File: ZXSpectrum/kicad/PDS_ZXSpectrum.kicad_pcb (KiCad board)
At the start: 2 copper layers, 73.7 x 70 mm, 15 parts, among them J2 PDS_IFACE, SW1 RESET, SW2 ENABLE, U1 Z8420 PIO, U2 74LS245, U3 74LS04

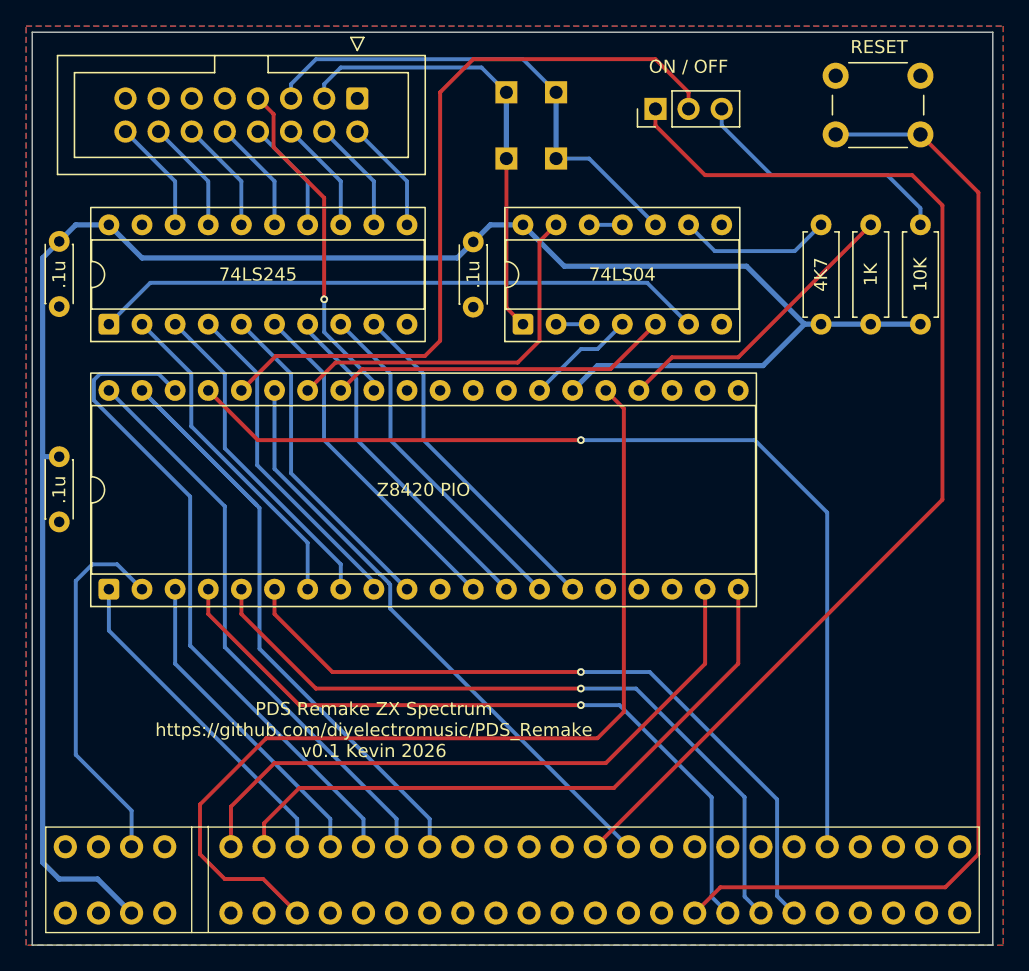
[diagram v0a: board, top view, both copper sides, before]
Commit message: Amstrad CPC
Added Amstrad CPC and updates Spectrum
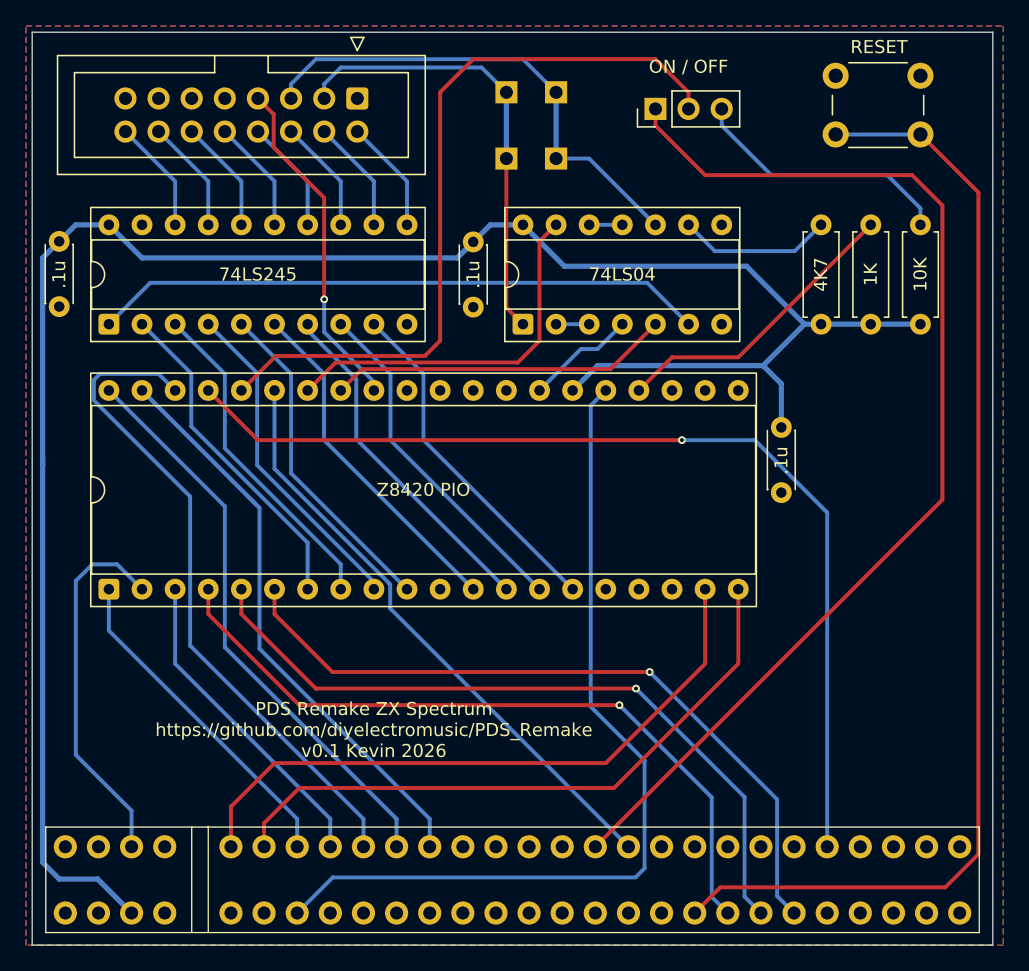
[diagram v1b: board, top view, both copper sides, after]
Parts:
- moved C1 55.4 mm to (107.4, 80.3)
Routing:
- net /CLOCK: track 73.8 -> 66.9 mm
- net VCC: track 150.2 -> 154.2 mm
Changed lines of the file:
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@@
 	(footprint "Capacitor_THT:C_Disc_D4.3mm_W1.9mm_P5.00mm"
 		(layer "F.Cu")
-		(at 52.07 82.55 -90)
+		(at 107.442 80.304 -90)
 		(descr "C, Disc series, Radial, pin pitch=5.00mm, diameter*width=4.3*1.9mm^2, Capacitor, http://www.vishay.com/docs/45233/krseries.pdf")
 		(tags "C Disc series Radial pin pitch 5.00mm diameter 4.3mm width 1.9mm Capacitor")
@@
 	)
 	(segment
+		(start 107.442 76.962)
+		(end 107.442 80.304)
+		(width 0.4)
+		(layer "B.Cu")
+		(net 1)
+	)
+	(segment
 		(start 58.42 67.31)
 		(end 55.88 64.77)
@@
 	)
 	(segment
+		(start 106.045 75.565)
+		(end 107.442 76.962)
+		(width 0.4)
+		(layer "B.Cu")
+		(net 1)
+	)
+	(segment
 		(start 82.59 67.31)
 		(end 58.42 67.31)
@@
 	)
 	(segment
-		(start 50.8 82.55)
-		(end 52.07 82.55)
-		(width 0.4)
-		(layer "B.Cu")
-		(net 1)
-	)
-	(segment
 		(start 85.13 64.77)
 		(end 83.82 66.08)
@@
 	)
 	(segment
+		(start 99.822 81.28)
+		(end 67.31 81.28)
+		(width 0.3)
+		(layer "F.Cu")
+		(net 4)
+	)
+	(segment
 		(start 67.31 81.28)
 		(end 63.5 77.47)
@@
 		(net 4)
 	)
-	(segment
-		(start 92.075 81.28)
-		(end 67.31 81.28)
-		(width 0.3)
-		(layer "F.Cu")
-		(net 4)
-	)
 	(via
-		(at 92.075 81.28)
+		(at 99.822 81.28)
 		(size 0.6)
 		(drill 0.3)
@@
 	)
 	(segment
+		(start 105.41 81.28)
+		(end 110.96 86.83)
+		(width 0.3)
+		(layer "B.Cu")
+		(net 4)
+	)
+	(segment
+		(start 99.822 81.28)
+		(end 105.41 81.28)
+		(width 0.3)
+		(layer "B.Cu")
+		(net 4)
+	)
+	(segment
 		(start 110.96 86.83)
-		(end 105.41 81.28)
-		(width 0.3)
-		(layer "B.Cu")
-		(net 4)
-	)
-	(segment
-		(start 110.96 112.46)
-		(end 110.96 86.83)
-		(width 0.3)
-		(layer "B.Cu")
-		(net 4)
-	)
-	(segment
-		(start 105.41 81.28)
-		(end 92.075 81.28)
+		(end 110.96 112.46)
 		(width 0.3)
 		(layer "B.Cu")
@@
 	)
 	(segment
+		(start 97.35 99.06)
+		(end 73.025 99.06)
+		(width 0.3)
+		(layer "F.Cu")
+		(net 12)
+	)
+	(segment
 		(start 73.025 99.06)
 		(end 68.58 94.615)
@@
 		(net 12)
 	)
-	(segment
-		(start 92.075 99.06)
-		(end 73.025 99.06)
-		(width 0.3)
-		(layer "F.Cu")
-		(net 12)
-	)
 	(via
-		(at 92.075 99.06)
+		(at 97.35 99.06)
 		(size 0.6)
 		(drill 0.3)
@@
 	)
 	(segment
-		(start 92.075 99.06)
-		(end 97.35 99.06)
+		(start 107.12 116.24)
+		(end 108.42 117.54)
+		(width 0.3)
+		(layer "B.Cu")
+		(net 12)
+	)
+	(segment
+		(start 97.35 99.06)
+		(end 107.12 108.83)
 		(width 0.3)
 		(layer "B.Cu")
@@
 	)
 	(segment
-		(start 107.12 116.24)
-		(end 108.42 117.54)
-		(width 0.3)
-		(layer "B.Cu")
-		(net 12)
-	)
-	(segment
-		(start 97.35 99.06)
-		(end 107.12 108.83)
-		(width 0.3)
-		(layer "B.Cu")
-		(net 12)
+		(start 96.3 100.33)
+		(end 71.755 100.33)
+		(width 0.3)
+		(layer "F.Cu")
+		(net 13)
+	)
+	(segment
+		(start 66.04 94.615)
+		(end 66.04 92.71)
+		(width 0.3)
+		(layer "F.Cu")
+		(net 13)
 	)
 	(segment
@@
 		(net 13)
 	)
-	(segment
-		(start 66.04 94.615)
-		(end 66.04 92.71)
-		(width 0.3)
-		(layer "F.Cu")
-		(net 13)
-	)
-	(segment
-		(start 92.075 100.33)
-		(end 71.755 100.33)
-		(width 0.3)
-		(layer "F.Cu")
-		(net 13)
-	)
 	(via
-		(at 92.075 100.33)
+		(at 96.3 100.33)
 		(size 0.6)
 		(drill 0.3)
@@
 	)
 	(segment
-		(start 92.075 100.33)
-		(end 96.3 100.33)
-		(width 0.3)
-		(layer "B.Cu")
-		(net 13)
-	)
-	(segment
 		(start 96.3 100.33)
 		(end 104.625 108.655)
@@
 	)
 	(segment
-		(start 67.715 114.935)
-		(end 64.77 114.935)
-		(width 0.3)
-		(layer "F.Cu")
+		(start 96.266 114.808)
+		(end 96.96 114.114)
+		(width 0.3)
+		(layer "B.Cu")
 		(net 14)
 	)
 	(segment
-		(start 93.345 104.14)
-		(end 95.369 102.116)
-		(width 0.3)
-		(layer "F.Cu")
+		(start 96.96 114.114)
+		(end 96.96 105.85)
+		(width 0.3)
+		(layer "B.Cu")
 		(net 14)
 	)
 	(segment
-		(start 62.865 109.22)
-		(end 67.945 104.14)
-		(width 0.3)
-		(layer "F.Cu")
+		(start 92.829 101.719)
+		(end 92.829 78.621)
+		(width 0.3)
+		(layer "B.Cu")
 		(net 14)
 	)
 	(segment
-		(start 64.77 114.935)
-		(end 62.865 113.03)
-		(width 0.3)
-		(layer "F.Cu")
+		(start 92.829 78.621)
+		(end 93.98 77.47)
+		(width 0.3)
+		(layer "B.Cu")
 		(net 14)
 	)
 	(segment
-		(start 95.369 102.116)
-		(end 95.369 78.859)
-		(width 0.3)
-		(layer "F.Cu")
+		(start 70.32 117.54)
+		(end 73.052 114.808)
+		(width 0.3)
+		(layer "B.Cu")
 		(net 14)
 	)
 	(segment
-		(start 95.369 78.859)
-		(end 93.98 77.47)
-		(width 0.3)
-		(layer "F.Cu")
+		(start 96.96 105.85)
+		(end 92.829 101.719)
+		(width 0.3)
+		(layer "B.Cu")
 		(net 14)
 	)
 	(segment
-		(start 70.32 117.54)
-		(end 67.715 114.935)
-		(width 0.3)
-		(layer "F.Cu")
-		(net 14)
-	)
-	(segment
-		(start 62.865 113.03)
-		(end 62.865 109.22)
-		(width 0.3)
-		(layer "F.Cu")
-		(net 14)
-	)
-	(segment
-		(start 67.945 104.14)
-		(end 93.345 104.14)
-		(width 0.3)
-		(layer "F.Cu")
+		(start 73.052 114.808)
+		(end 96.266 114.808)
+		(width 0.3)
+		(layer "B.Cu")
 		(net 14)
 	)
@@
 	)
 	(segment
+		(start 70.485 101.6)
+		(end 63.5 94.615)
+		(width 0.3)
+		(layer "F.Cu")
+		(net 18)
+	)
+	(segment
+		(start 95.03 101.6)
+		(end 70.485 101.6)
+		(width 0.3)
+		(layer "F.Cu")
+		(net 18)
+	)
+	(segment
 		(start 63.5 94.615)
 		(end 63.5 92.71)
@@
 		(net 18)
 	)
-	(segment
-		(start 92.075 101.6)
-		(end 70.485 101.6)
-		(width 0.3)
-		(layer "F.Cu")
-		(net 18)
-	)
-	(segment
-		(start 70.485 101.6)
-		(end 63.5 94.615)
-		(width 0.3)
-		(layer "F.Cu")
-		(net 18)
-	)
 	(via
-		(at 92.075 101.6)
+		(at 95.03 101.6)
 		(size 0.6)
 		(drill 0.3)
@@
 	)
 	(segment
+		(start 102.1 116.3)
+		(end 103.34 117.54)
+		(width 0.3)
+		(layer "B.Cu")
+		(net 18)
+	)
+	(segment
+		(start 95.03 101.6)
+		(end 102.1 108.67)
+		(width 0.3)
+		(layer "B.Cu")
+		(net 18)
+	)
+	(segment
 		(start 102.1 108.67)
 		(end 102.1 116.3)
 		(width 0.3)
 		(layer "B.Cu")
-		(net 18)
-	)
-	(segment
-		(start 92.075 101.6)
-		(end 95.03 101.6)
-		(width 0.3)
-		(layer "B.Cu")
-		(net 18)
-	)
-	(segment
-		(start 102.1 116.3)
-		(end 103.34 117.54)
-		(width 0.3)
-		(layer "B.Cu")
-		(net 18)
-	)
-	(segment
-		(start 95.03 101.6)
-		(end 102.1 108.67)
-		(width 0.3)
-		(layer "B.Cu")
